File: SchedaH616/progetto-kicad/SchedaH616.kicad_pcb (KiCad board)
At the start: 6 copper layers, 50 x 70 mm, 329 parts, among them J1 BUS_POWER_MIKILAB, J103 DC-005-5A-2.0, J104 TYPE-C-31-M-12, J2 BUS_MIKILAB_MAIN, J301 UART0 debug, J401 DM3AT-SF-PEJM5, J501 HR911130C, J601 U.FL, J701 SMA antenna, J702 SMA PPS OUT, J703 SMA STROBE IN, J704 PPS/STROBE, J801 TYPE-C-31-M-12, SW301 RESET, SW302 FEL, U101 TPS56637RPAR, U103 TPS2121RUXR, U104 FUSB302BMPX, U105 SY6280AAC, U106 TPS259470ARPWR, U107 TPD2EUSB30ADRTR, U201 AXP313A, U202 TPS563201DDCR, U203 AP2112K-1.8TRG1, U301 H616, U302 TPD4E05U06DQA, U303 TPD4E05U06DQA, U304 TPD4E05U06DQA, U305 TPD4E05U06DQA, U306 TPD4E05U06DQA, U307 TPD4E05U06DQA, U308 TCA6416APWR, U401 MT53E512M32D1ZW-046 IT:B, U402 eMMC 64GB, U403 TPD4E05U06DQA, U404 TPD4E05U06DQA, U501 RTL8211F-CG, U502 25AA02E48T-I/OT, U601 AP6256, U701 NEO-M9N-00B, U702 74LVC1G17, U703 74LVC1G17, U801 TPS2553DBVR, U802 USBLC6-2SC6, Y301 24MHz, Y501 25MHz

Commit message: SchedaH616: secondo TPS2121 tra buck e jack, controlli dalla Orange Pi Zero2
- TPS2121 U108: IN1 = 5V_BUCK (priorita), IN2 = jack, uscita 5V_EXT verso U103 (IN2 = USB-C)
  PR1 4.49 V, CP2 a GND, OV 5.98 V, ILM 22.1k, ST con test point; priorita bus > jack > USB-C
- TPS56637 di nuovo in FCCM (R114 DNP): il buck ora e' isolato dal jack
- Dalla Orange Pi Zero2 v1.3: REXT 150k 1% ad AGND, AVCC e AC_AVCC 2.2 uF; AC_VRA1 su C17 confermato
- PCB aggiornato: U108 vicino a U103 e al jack
- ERC 0, parita' schema/PCB 0, DRC 0 (solo collegamenti da fare)

Co-Authored-By: Claude Opus 5.5 (1M context) <noreply@anthropic.com>
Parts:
- added C132: 100nF, Capacitor_SMD:C_0603_1608Metric, B.Cu at (117.8, 121.0)
- added C133: 1uF/10V, Capacitor_SMD:C_0603_1608Metric, B.Cu at (119.6, 118.5)
- added C134: 1uF/10V, Capacitor_SMD:C_0603_1608Metric, B.Cu at (112.0, 119.5)
- added C135: 10uF/10V, Capacitor_SMD:C_0805_2012Metric, B.Cu at (117.0, 108.0)
- added C334: 2.2uF/6.3V, Capacitor_SMD:C_0402_1005Metric, B.Cu at (128.5, 132.0)
- added C335: 2.2uF/6.3V, Capacitor_SMD:C_0402_1005Metric, B.Cu at (118.8, 132.2)
- added R121: 32.4k 1%, Resistor_SMD:R_0603_1608Metric, B.Cu at (108.2, 127.2)
- added R122: 10k 1%, Resistor_SMD:R_0603_1608Metric, B.Cu at (103.8, 129.0)
- added R123: 46.4k 1%, Resistor_SMD:R_0603_1608Metric, B.Cu at (115.5, 128.2)
- added R124: 10k 1%, Resistor_SMD:R_0603_1608Metric, B.Cu at (116.8, 130.0)
- added R125: 46.4k 1%, Resistor_SMD:R_0603_1608Metric, B.Cu at (104.5, 119.8)
- added R126: 10k 1%, Resistor_SMD:R_0603_1608Metric, B.Cu at (102.8, 120.0)
- added R127: 22.1k 1%, Resistor_SMD:R_0603_1608Metric, F.Cu at (115.5, 131.5)
- added R128: 100k, Resistor_SMD:R_0603_1608Metric, B.Cu at (116.5, 132.0)
- added R337: 150k 1%, Resistor_SMD:R_0402_1005Metric, B.Cu at (126.5, 132.5)
- added TP101: MUX2_ST, TestPoint:TestPoint_Pad_D1.0mm, B.Cu at (117.8, 134.5)
- added U108: TPS2121RUXR, Package_DFN_QFN:Texas_VQFN-HR-12_2x2.5mm_P0.5mm, B.Cu at (117.0, 118.5)
- C106, C416, C417, C423, C606, R120, R3, R310, R320, R407, R412, R415, R416, R601: moved to F.Cu
- C126, C601, C604, R115, R116, R117, R317, R318, R326, R413, R414, R602: moved to B.Cu
- moved R320 35.5 mm to (141.5, 104.0), turned to 90 degrees
- moved R115 32.4 mm to (115.6, 126.5)
- moved R116 25.4 mm to (131.5, 126.8), turned to 0 degrees
- moved R104 25.4 mm to (118.0, 126.5), turned to 90 degrees
- moved R103 25.2 mm to (135.2, 126.2), turned to 0 degrees
- moved R327 24.3 mm to (142.2, 126.2)
- moved C127 23.0 mm to (122.8, 116.0)
- moved R319 22.3 mm to (102.5, 122.8)
- moved R326 22.3 mm to (142.2, 126.2)
- moved C105 22.0 mm to (123.1, 112.3)
- moved R3 21.3 mm to (140.4, 101.9)
- moved C128 20.5 mm to (122.8, 118.5), turned to 0 degrees
- moved R312 20.3 mm to (137.5, 126.2), turned to 90 degrees
- moved C423 19.8 mm to (140.4, 106.7)
- moved R314 19.5 mm to (111.5, 124.8), turned to 90 degrees
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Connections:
- C104 pad 1: /Alimentazione/5V_EXT -> /Alimentazione/5V_BUCK
- C105 pad 1: /Alimentazione/5V_EXT -> /Alimentazione/5V_BUCK
- C106 pad 1: /Alimentazione/5V_EXT -> /Alimentazione/5V_JACK
- C127 pad 1: /Alimentazione/5V_EXT -> /Alimentazione/5V_BUCK
- C128 pad 1: /Alimentazione/5V_EXT -> /Alimentazione/5V_BUCK
- D101 pad 1: /Alimentazione/5V_EXT -> /Alimentazione/5V_JACK
- J103 pad 1: /Alimentazione/5V_EXT -> /Alimentazione/5V_JACK
- L101 pad 2: /Alimentazione/5V_EXT -> /Alimentazione/5V_BUCK
- R103 pad 1: /Alimentazione/5V_EXT -> /Alimentazione/5V_BUCK
- R115 pad 1: /Alimentazione/5V_EXT -> /Alimentazione/5V_BUCK
- R116 pad 1: /Alimentazione/5V_EXT -> /Alimentazione/5V_BUCK
- U301 pad K18: unconnected-(U301D-REXT-PadK18) -> /CPU/SOC_REXT

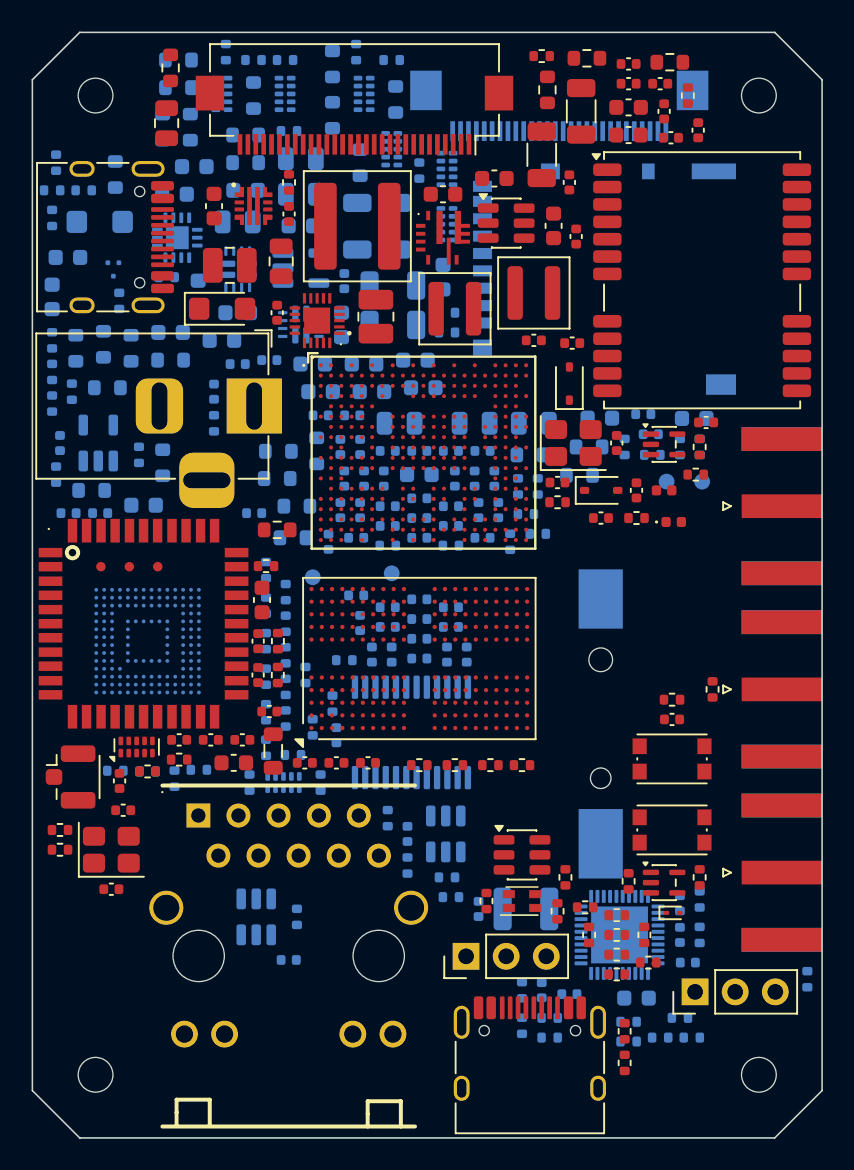
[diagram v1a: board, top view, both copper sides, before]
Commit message: SchedaH616: verifica sullo schema Orange Pi Zero3 (LPDDR4, AXP313A, reset)
- Mappa CA/CS/CK/CKE/RESET della LPDDR4 verificata 8/8 sulla Zero3, sfere della LPDDR4, ODT 100k e ZQ 240R coincidono
- AXP313A allineato alla Zero3: 22 uF sui VIN, 2x47 uF + 1 uF + 100 nF sulle uscite DCDC, DLDO1 47 uF, RTCLDO 4.7 uF, PWRON 100 nF montato
- DCDC3 a 1.1 V impostato dall'SPL di U-Boot (CONFIG_AXP_DCDC3_VOLT)
- RESET H616: 10k a VCC-1V8, 1 nF, 100R in serie da AP-RESET; AC_AVCC 10 uF; quarzo 24 MHz con 12 pF
- scelte-progetto.md: verifiche segnate, differenze volute (VCC_PG 3.3 V, VCC_PC 1.8 V), nuovo punto aperto sugli strap BOOT_SEL
- ERC 0, parita' 0, DRC 0 (solo collegamenti da fare)

Co-Authored-By: Claude Opus 5.5 (1M context) <noreply@anthropic.com>
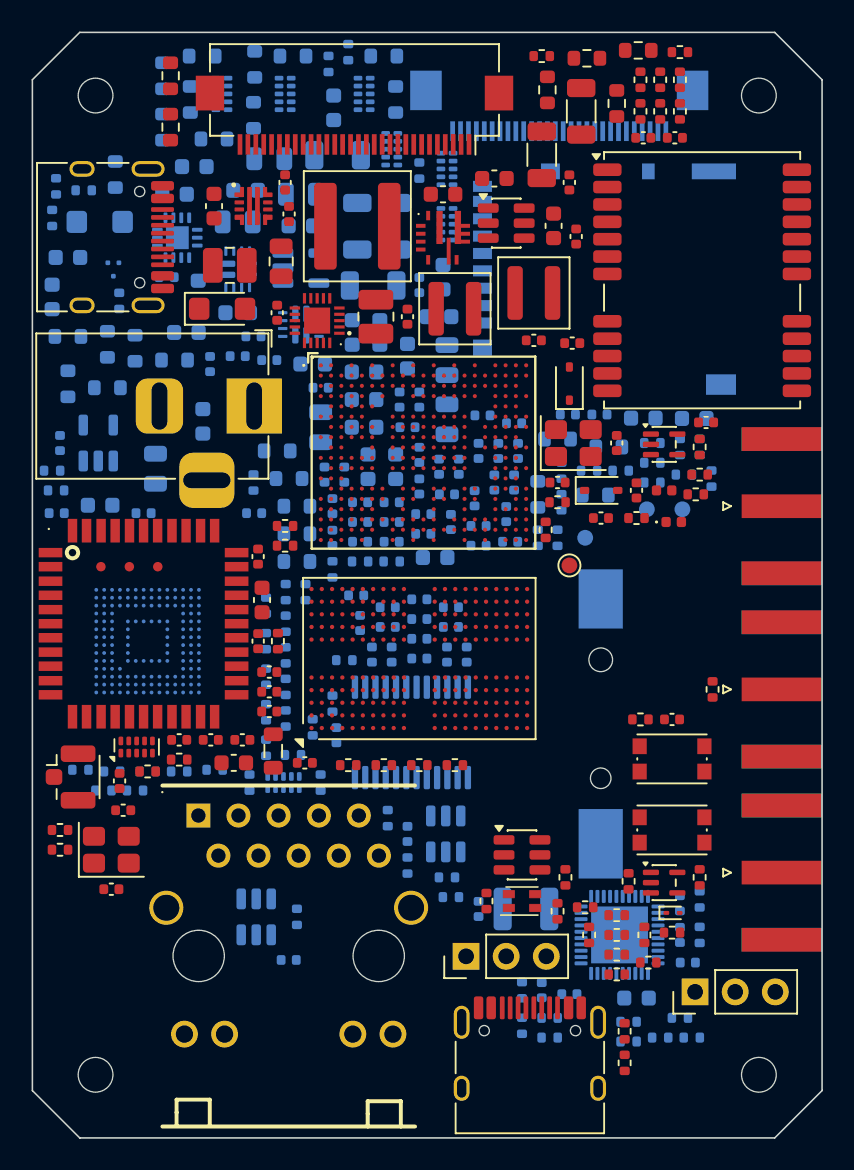
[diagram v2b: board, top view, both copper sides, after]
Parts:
- added C224: 1uF, Capacitor_SMD:C_0402_1005Metric, F.Cu at (116.0, 109.5)
- added C225: 1uF, Capacitor_SMD:C_0402_1005Metric, B.Cu at (124.5, 116.0)
- added C226: 100nF, Capacitor_SMD:C_0402_1005Metric, B.Cu at (124.5, 123.2)
- added C227: 100nF, Capacitor_SMD:C_0402_1005Metric, B.Cu at (108.5, 115.5)
- added C228: 100nF, Capacitor_SMD:C_0402_1005Metric, B.Cu at (128.5, 124.2)
- added C229: 47uF/6.3V, Capacitor_SMD:C_0603_1608Metric, B.Cu at (121.0, 125.0)
- added C230: 100nF, Capacitor_SMD:C_0402_1005Metric, B.Cu at (123.8, 125.0)
- added C231: 4.7uF/10V, Capacitor_SMD:C_0402_1005Metric, B.Cu at (111.3, 121.0)
- added R338: 100R, Resistor_SMD:R_0402_1005Metric, B.Cu at (139.2, 128.5)
- added R339: 10k, Resistor_SMD:R_0402_1005Metric, F.Cu at (138.5, 143.5)
- C106, C305, C306, C307, C308, C309, C603, C702, C705, R120, R127, R201, R310, R320, R327, R412, R415, R416, R601: moved to B.Cu
- C201, C202, C203: value 10uF/10V -> 22uF/10V
- C208, C209, C210, C212: value 22uF/6.3V -> 47uF/6.3V
- C211: value 22uF/6.3V -> 47uF/6.3V; moved to B.Cu
- C213: value 22uF/6.3V -> 1uF; footprint Capacitor_SMD:C_0603_1608Metric -> Capacitor_SMD:C_0402_1005Metric; moved to F.Cu
- C215: value 4.7uF/10V -> 47uF/6.3V; footprint Capacitor_SMD:C_0402_1005Metric -> Capacitor_SMD:C_0603_1608Metric
- C301, C302: value 18pF/50V -> 12pF/50V
- C335: value 2.2uF/6.3V -> 10uF/6.3V; footprint Capacitor_SMD:C_0402_1005Metric -> Capacitor_SMD:C_0603_1608Metric
- C418, C601, C706, R112, R114, R117, R202, R203, R204, R205, R308, R313, R314, R319, R326, R328, R332, R336, R413, R414, R705, TP201: moved to F.Cu
- moved R322 40.1 mm to (137.2, 127.8)
- moved R319 39.9 mm to (142.2, 126.2)
- moved R321 39.0 mm to (135.2, 127.8), turned to 0 degrees
- moved R318 37.9 mm to (142.2, 126.2)
- moved R314 37.7 mm to (141.0, 101.2), turned to 0 degrees
- moved R201 37.1 mm to (124.5, 108.8), turned to 90 degrees
- moved R323 34.5 mm to (141.2, 128.0), turned to 0 degrees
- moved R317 32.9 mm to (139.2, 127.2)
- moved R335 32.0 mm to (133.5, 129.8)
- moved C307 29.7 mm to (124.5, 128.8), turned to 90 degrees
- moved C309 29.6 mm to (126.2, 129.2)
- moved C305 27.1 mm to (123.0, 127.5), turned to 90 degrees
- moved C306 27.1 mm to (125.8, 127.5), turned to 90 degrees
- moved C308 26.0 mm to (127.0, 127.5)
- moved R320 25.1 mm to (133.5, 127.8)
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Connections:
- C304 pad 1: /AP-RESET -> /CPU/SOC_RESET
- SW301 pad 1: /AP-RESET -> /CPU/SOC_RESET
- U201 pad 7: unconnected-(U201-RTCLDO-Pad7) -> /PMIC/PMU_RTCLDO
- U301 pad A16: /AP-RESET -> /CPU/SOC_RESET

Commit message: SchedaH616: footprint DNP per gli strap BOOT_SEL (PC3-PC6)
- Nessuno strap montato, come la Orange Pi Zero2
- 10k DNP di pull-up (VCC_PC) e pull-down (GND) su PC3, PC4, PC5 (EMMC_CLK), PC6 (EMMC_CMD): R340-R347
- scelte-progetto.md: ordine di boot non verificato, serve lo User Manual H616 §3.4
- ERC 0, parita' 0, DRC 0 (solo collegamenti da fare)

Co-Authored-By: Claude Opus 5.5 (1M context) <noreply@anthropic.com>
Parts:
- added R340: 10k, Resistor_SMD:R_0402_1005Metric, B.Cu at (132.0, 133.2)
- added R341: 10k, Resistor_SMD:R_0402_1005Metric, B.Cu at (133.8, 132.8)
- added R342: 10k, Resistor_SMD:R_0402_1005Metric, B.Cu at (118.8, 134.2)
- added R343: 10k, Resistor_SMD:R_0402_1005Metric, B.Cu at (118.8, 136.2)
- added R344: 10k, Resistor_SMD:R_0402_1005Metric, F.Cu at (133.0, 132.2)
- added R345: 10k, Resistor_SMD:R_0402_1005Metric, F.Cu at (134.0, 133.5)
- added R346: 10k, Resistor_SMD:R_0402_1005Metric, B.Cu at (114.8, 139.5)
- added R347: 10k, Resistor_SMD:R_0402_1005Metric, B.Cu at (116.0, 139.5)
- C126, C422, C603, C705, R104, R120, R320, R322, R327, R338, R406, R408, R409, TP101: moved to F.Cu
- C418, C423, C606, R114, R117, R202, R203, R308, R313, R314, R319, R328, R332, R407, TP201: moved to B.Cu
- moved R318 40.6 mm to (103.0, 115.8), turned to 0 degrees
- moved R319 40.6 mm to (102.2, 119.2)
- moved R321 35.9 mm to (101.2, 116.2), turned to 90 degrees
- moved R317 35.3 mm to (105.5, 117.0), turned to 90 degrees
- moved R325 33.1 mm to (134.5, 126.8)
- moved R127 31.8 mm to (131.8, 131.0), turned to 90 degrees
- moved R308 30.5 mm to (103.0, 110.0)
- moved R320 26.2 mm to (140.5, 102.5)
- moved R116 25.9 mm to (122.2, 101.5)
- moved R326 25.5 mm to (141.7, 102.5), turned to 90 degrees
- moved R314 25.0 mm to (134.7, 125.5)
- moved R104 24.5 mm to (135.0, 101.8)
- moved R115 24.5 mm to (114.6, 126.5), turned to 0 degrees
- moved R103 23.8 mm to (123.0, 104.2), turned to 90 degrees
- moved R322 23.6 mm to (141.0, 104.5), turned to 90 degrees
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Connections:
- U301 pad D1: unconnected-(U301B-PC3-PadD1) -> /CPU/SOC_BOOT_SEL1
- U301 pad D2: unconnected-(U301B-PC4-PadD2) -> /CPU/SOC_BOOT_SEL2

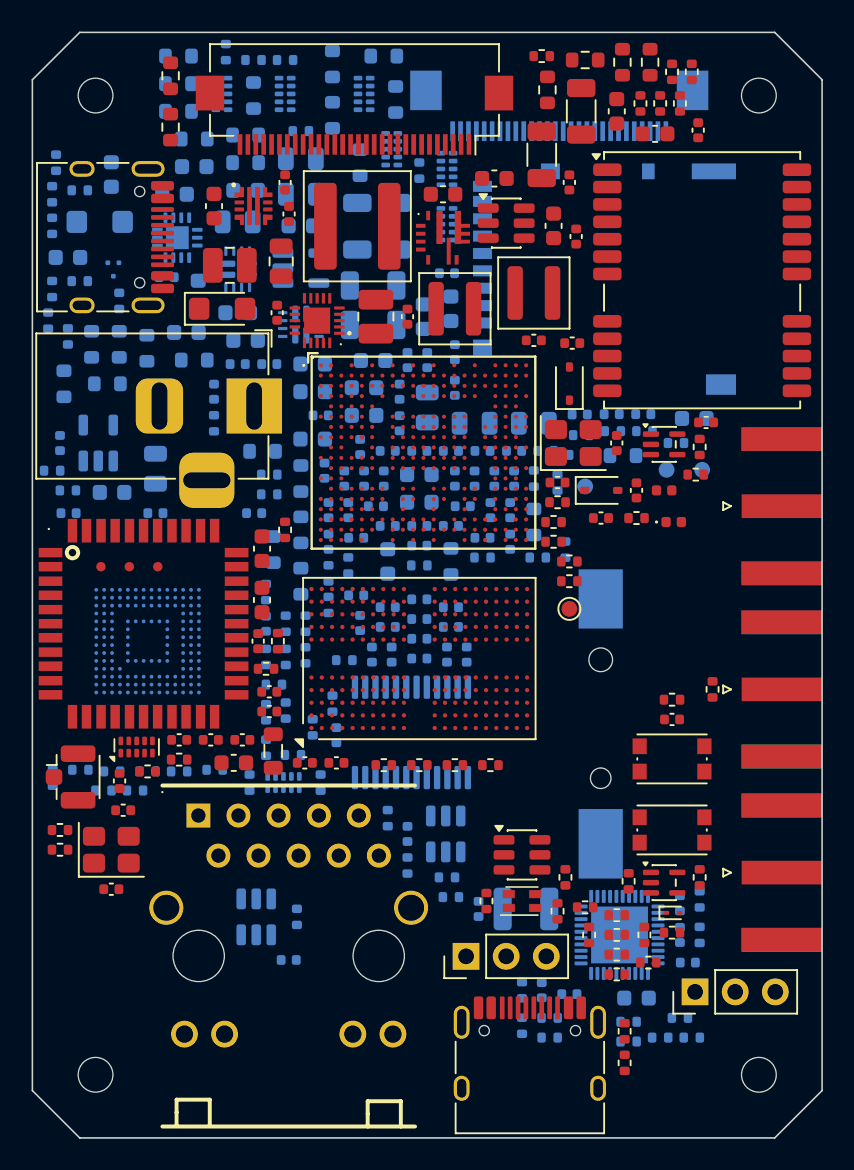
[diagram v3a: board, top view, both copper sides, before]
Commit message: SchedaH616: eMMC FORESEE FEMDNN064G-C9A61 (LCSC C49284704)
- U402: valore, MPN e campo LCSC; pinout verificato sul datasheet FORESEE (fig. 2), package JEDEC MO-276 11.5x13 passo 0.5, footprint invariato
- aggiunte a GND le sfere VSS A6 e J5, che mancavano nel simbolo
- campo LCSC portato anche sul PCB; README e scelte-progetto.md aggiornati
- ERC 0, parita' 0, DRC 0 (solo collegamenti da fare)

Co-Authored-By: Claude Opus 5.5 (1M context) <noreply@anthropic.com>
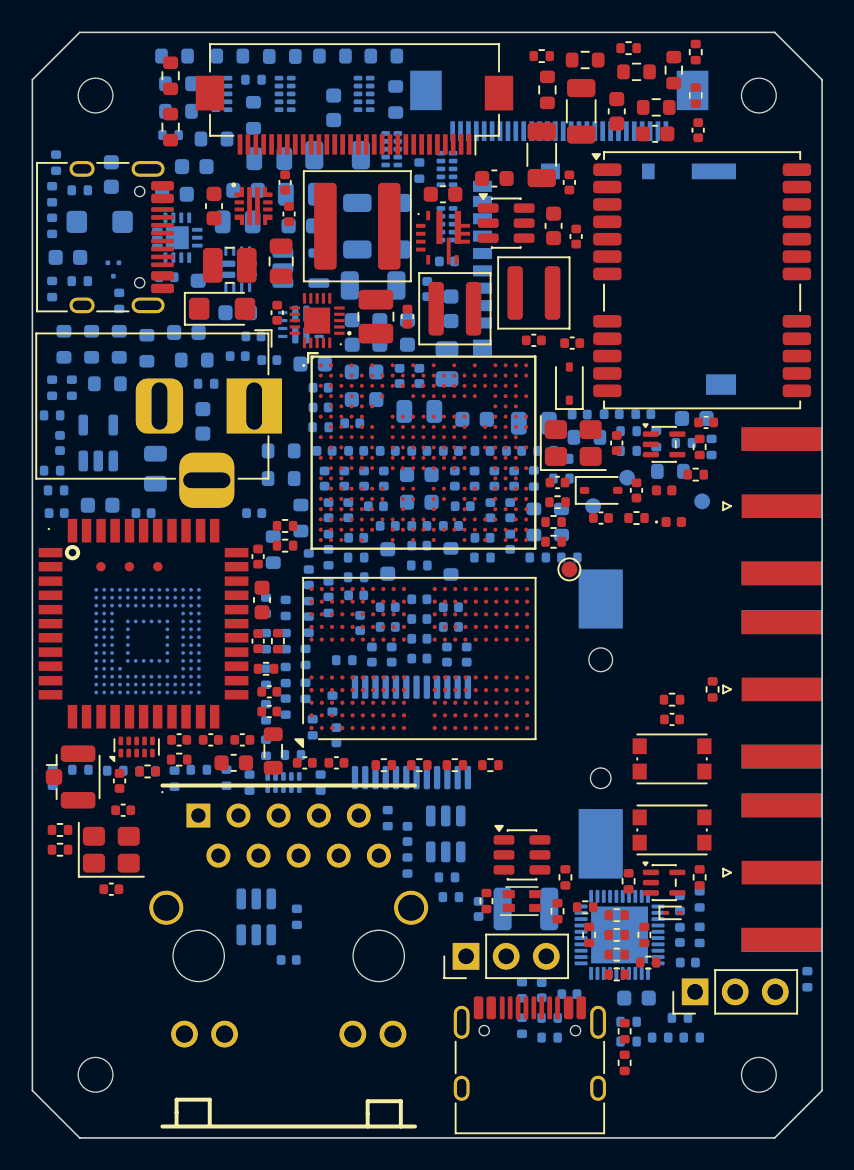
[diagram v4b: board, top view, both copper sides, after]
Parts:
- C603, R120, R3, R311, R322, R327, R338, R344, R345, R406, R413, R414, R705: moved to B.Cu
- C606, R103, R116, R118, R203, R328, R334, R405, R415, R416: moved to F.Cu
- U402: value eMMC 64GB -> FEMDNN064G-C9A61
- moved R322 44.4 mm to (101.2, 124.2), turned to 0 degrees
- moved R324 34.6 mm to (134.5, 127.0), turned to 0 degrees
- moved R325 33.3 mm to (101.2, 127.8)
- moved R127 31.8 mm to (102.0, 119.8)
- moved R311 29.7 mm to (111.0, 122.2)
- moved R115 25.0 mm to (115.8, 101.5)
- moved R3 24.1 mm to (135.1, 125.6), turned to 0 degrees
- moved R326 23.8 mm to (142.2, 126.2)
- moved R607 18.7 mm to (101.3, 147.2)
- moved R116 17.6 mm to (139.5, 104.8)
- moved R126 16.9 mm to (133.5, 131.0)
- moved R124 16.9 mm to (115.2, 132.8)
- moved R329 16.8 mm to (131.8, 128.2), turned to 90 degrees
- moved R406 16.7 mm to (117.5, 137.5), turned to 90 degrees
- moved R125 16.6 mm to (131.8, 131.0)
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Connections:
- U402 pad A6: (no net) -> GND_D
- U402 pad J5: (no net) -> GND_D
